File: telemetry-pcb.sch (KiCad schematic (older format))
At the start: 44 parts, among them CN1 12V_IN, CN10 THERMO1, CN11 THERMO2, CN12 RS232, CN13 CAN, CN14 CAN, CN15 12V_OUT, CN16 12V_OUT, CN2 12V_OUT, CN3 12V_OUT, CN5 ACC_12V_CAN, CN6 CAN, CN7 CAN, CN8 CAN, CN9 CAN, IC1 MAX31855K, IC2 MAX31855K, IC3 TCAN332DR, IC4 MAX3232CPWR, M1 MountingHole, M2 MountingHole, M3 MountingHole, M4 MountingHole, T1 TEST_12V, T2 TEST_3V3, T3 TEST_CAN, T4 GPIO1, T5 GPIO2, T6 TEST_RS232

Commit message: finished first draft of PCB
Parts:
- CN10: renamed from CN13; footprint (none) -> Conn_Molex_70553-0001:Molex-70553-0001-0-0-MFG
- CN11: renamed from CN14; footprint (none) -> Conn_Molex_70553-0001:Molex-70553-0001-0-0-MFG
- CN13: renamed from CN10; footprint (none) -> Conn_Molex_70553-0002:Molex-70553-0002-0-0-0; symbol Connector_Generic:Conn_01x02 -> Connector_Generic:Conn_01x03
- CN14: renamed from CN11; footprint (none) -> Conn_Molex_70553-0002:Molex-70553-0002-0-0-0; symbol Connector_Generic:Conn_01x02 -> Connector_Generic:Conn_01x03
- CN6, CN7, CN8, CN9: footprint (none) -> Conn_Molex_70553-0001:Molex-70553-0001-0-0-MFG
- renumbered CN5 to CN12, CN12 to CN15, CN15 to CN4, CN16 to CN5
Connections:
- wire segments 261 -> 259
- no-connect marks 16 -> 18
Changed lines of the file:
@@
 	10100 7150 10100 5750
 $Comp
-L Connector:DB9_Male CN12
+L Connector:DB9_Male CN15
 U 1 1 600D7019
 P 10950 5650
-F 0 "CN12" H 11130 5696 50  0000 L CNN
+F 0 "CN15" H 11130 5696 50  0000 L CNN
 F 1 "RS232" H 11130 5605 50  0000 L CNN
 F 2 "Connector_Dsub:DSUB-9_Male_Horizontal_P2.77x2.54mm_EdgePinOffset9.40mm" H 10950 5650 50  0001 C CNN
@@
 	4950 2500 5700 2500
 Wire Wire Line
-	5250 550  5750 550
-Wire Wire Line
-	6500 1600 6500 850
-Wire Wire Line
-	6500 850  6250 850
-Wire Wire Line
-	6500 850  6500 650
-Wire Wire Line
-	6500 650  6250 650
-Connection ~ 6500 850
-Wire Wire Line
 	8050 2750 8050 2050
-Wire Wire Line
-	6650 1450 6650 750
-Wire Wire Line
-	6650 750  6250 750
 Connection ~ 8050 2750
 Wire Wire Line
-	6650 750  6650 550
-Wire Wire Line
 	6650 550  6250 550
-Connection ~ 6650 750
 $Comp
 L Connector_Generic:Conn_01x02 CN3
@@
 F 0 "CN6" V 7314 112 50  0000 R CNN
 F 1 "CAN" V 7223 112 50  0000 R CNN
-F 2 "" H 7350 300 50  0001 C CNN
+F 2 "Conn_Molex_70553-0001:Molex-70553-0001-0-0-MFG" H 7350 300 50  0001 C CNN
 F 3 "~" H 7350 300 50  0001 C CNN
 	1    7350 300
@@
 F 0 "CN7" V 8114 112 50  0000 R CNN
 F 1 "CAN" V 8023 112 50  0000 R CNN
-F 2 "" H 8150 300 50  0001 C CNN
+F 2 "Conn_Molex_70553-0001:Molex-70553-0001-0-0-MFG" H 8150 300 50  0001 C CNN
 F 3 "~" H 8150 300 50  0001 C CNN
 	1    8150 300
@@
 F 0 "CN8" V 8864 112 50  0000 R CNN
 F 1 "CAN" V 8773 112 50  0000 R CNN
-F 2 "" H 8900 300 50  0001 C CNN
+F 2 "Conn_Molex_70553-0001:Molex-70553-0001-0-0-MFG" H 8900 300 50  0001 C CNN
 F 3 "~" H 8900 300 50  0001 C CNN
 	1    8900 300
@@
 F 0 "CN9" V 9614 112 50  0000 R CNN
 F 1 "CAN" V 9523 112 50  0000 R CNN
-F 2 "" H 9650 300 50  0001 C CNN
+F 2 "Conn_Molex_70553-0001:Molex-70553-0001-0-0-MFG" H 9650 300 50  0001 C CNN
 F 3 "~" H 9650 300 50  0001 C CNN
 	1    9650 300
@@
 Wire Wire Line
 	1300 500  1300 700
-Wire Wire Line
-	2150 500  2150 1200
-Wire Wire Line
-	3000 500  3000 1200
-Connection ~ 2150 1200
-Wire Wire Line
-	2250 1350 2250 500
 Connection ~ 1600 1350
 Wire Wire Line
 	1600 1350 1600 1500
-Wire Wire Line
-	3100 1350 3100 500
-Connection ~ 2250 1350
 $Comp
 L Connector:Conn_01x02_Female T3
@@
 	4950 1900 4950 2050
 $Comp
-L Connector_Generic:Conn_02x05_Counter_Clockwise CN5
+L Connector_Generic:Conn_02x05_Counter_Clockwise CN12
 U 1 1 601BCF89
 P 5950 750
-F 0 "CN5" H 6000 1167 50  0000 C CNN
+F 0 "CN12" H 6000 1167 50  0000 C CNN
 F 1 "ACC_12V_CAN" H 6000 1076 50  0000 C CNN
 F 2 "Connector_Molex:Molex_Mega-Fit_76825-0010_2x05_P5.70mm_Horizontal" H 5950 750 50  0001 C CNN
@@
 	1    0    0    -1
 $EndComp
-Wire Wire Line
-	5250 650  5750 650
-Wire Wire Line
-	5250 750  5750 750
-Wire Wire Line
-	5500 850  5750 850
-Wire Wire Line
-	5500 950  5750 950
-Connection ~ 5500 950
-Wire Wire Line
-	5500 950  5500 850
-$Comp
-L Connector_Generic:Conn_01x02 CN13
+$Comp
+L Connector_Generic:Conn_01x02 CN10
 U 1 1 6024B164
 P 10350 300
-F 0 "CN13" V 10314 112 50  0000 R CNN
+F 0 "CN10" V 10314 112 50  0000 R CNN
 F 1 "CAN" V 10223 112 50  0000 R CNN
-F 2 "" H 10350 300 50  0001 C CNN
+F 2 "Conn_Molex_70553-0001:Molex-70553-0001-0-0-MFG" H 10350 300 50  0001 C CNN
 F 3 "~" H 10350 300 50  0001 C CNN
 	1    10350 300
@@
 $EndComp
 $Comp
-L Connector_Generic:Conn_01x02 CN14
+L Connector_Generic:Conn_01x02 CN11
 U 1 1 6024BB8E
 P 11000 300
-F 0 "CN14" V 10964 112 50  0000 R CNN
+F 0 "CN11" V 10964 112 50  0000 R CNN
 F 1 "CAN" V 10873 112 50  0000 R CNN
-F 2 "" H 11000 300 50  0001 C CNN
+F 2 "Conn_Molex_70553-0001:Molex-70553-0001-0-0-MFG" H 11000 300 50  0001 C CNN
 F 3 "~" H 11000 300 50  0001 C CNN
 	1    11000 300
@@
 $EndComp
 $Comp
-L Connector_Generic:Conn_01x02 CN15
+L Connector_Generic:Conn_01x02 CN4
 U 1 1 6035BAD8
 P 3800 300
-F 0 "CN15" V 3764 112 50  0000 R CNN
+F 0 "CN4" V 3764 112 50  0000 R CNN
 F 1 "12V_OUT" V 3673 112 50  0000 R CNN
 F 2 "Connector_Molex:Molex_Mega-Fit_76825-0002_2x01_P5.70mm_Horizontal" H 3800 300 50  0001 C CNN
@@
 	0    -1   -1   0
 $EndComp
-Wire Wire Line
-	3000 1200 3800 1200
-Wire Wire Line
-	3800 1200 3800 500
-Connection ~ 3000 1200
-Wire Wire Line
-	3100 1350 3900 1350
-Connection ~ 3100 1350
 NoConn ~ 10650 5250
 NoConn ~ 10650 5350
@@
 Connection ~ 4950 2500
 Wire Wire Line
-	3900 500  3900 1350
-Wire Wire Line
-	5500 950  5500 1350
-Wire Wire Line
-	6250 1350 5500 1350
-Wire Wire Line
-	6250 950  6250 1350
-Wire Wire Line
-	3800 1200 4600 1200
-Connection ~ 3800 1200
-Wire Wire Line
 	3000 5500 3000 6200
 Wire Wire Line
@@
 Wire Wire Line
 	3050 6000 2500 6000
-Wire Wire Line
-	2500 6000 2500 5800
 Connection ~ 3050 6000
 $Comp
@@
 Wire Wire Line
 	3050 4900 2500 4900
-Wire Wire Line
-	2500 4900 2500 4700
 Connection ~ 3050 4900
 Wire Wire Line
@@
 	8050 1450 7450 1450
 $Comp
-L Connector_Generic:Conn_01x02 CN16
+L Connector_Generic:Conn_01x02 CN5
 U 1 1 603106BF
 P 4600 300
-F 0 "CN16" V 4564 112 50  0000 R CNN
+F 0 "CN5" V 4564 112 50  0000 R CNN
 F 1 "12V_OUT" V 4473 112 50  0000 R CNN
 F 2 "Connector_Molex:Molex_Mega-Fit_76825-0002_2x01_P5.70mm_Horizontal" H 4600 300 50  0001 C CNN
@@
 	0    -1   -1   0
 $EndComp
-Wire Wire Line
-	4600 500  4600 1200
-Wire Wire Line
-	3900 1350 4700 1350
-Connection ~ 3900 1350
-Wire Wire Line
-	4700 500  4700 1350
-Wire Wire Line
-	4600 1200 5250 1200
-Wire Wire Line
-	5250 1200 5250 750
-Connection ~ 4600 1200
-Connection ~ 5250 650
-Wire Wire Line
-	5250 650  5250 550
-Connection ~ 5250 750
-Wire Wire Line
-	5250 750  5250 650
-Wire Wire Line
-	4700 1350 5500 1350
-Connection ~ 4700 1350
-Connection ~ 5500 1350
 Wire Wire Line
 	1400 500  1400 600
@@
 $EndComp
 $Comp
-L Connector_Generic:Conn_01x02 CN10
+L Connector_Generic:Conn_01x03 CN14
+U 1 1 601BC25C
+P 2300 5800
+F 0 "CN14" V 2264 5612 50  0000 R CNN
+F 1 "THERMO2" V 2173 5612 50  0000 R CNN
+F 2 "Conn_Molex_70553-0002:Molex-70553-0002-0-0-0" H 2300 5800 50  0001 C CNN
+F 3 "~" H 2300 5800 50  0001 C CNN
+	1    2300 5800
+	-1   0    0    1
+$EndComp
+Connection ~ 1400 700
+Wire Wire Line
+	1400 1000 1400 1200
+Wire Wire Line
+	1200 1350 1200 500
+Wire Wire Line
+	1200 1350 1100 1350
+Connection ~ 1200 1350
+Wire Wire Line
+	1100 500  1100 600
+Wire Wire Line
+	750  1350 1100 1350
+Connection ~ 1100 1350
+Wire Wire Line
+	750  1250 750  1200
+Wire Wire Line
+	750  1200 1400 1200
+Connection ~ 1400 1200
+Connection ~ 1400 600
+Wire Wire Line
+	1400 600  1400 700
+Connection ~ 1100 600
+Wire Wire Line
+	1100 600  1100 1350
+Wire Wire Line
+	1400 1200 1850 1200
+Wire Wire Line
+	1850 1100 1850 1200
+Connection ~ 1850 1200
+Wire Wire Line
+	2500 4800 2500 4900
+Wire Wire Line
+	2500 5900 2500 6000
+NoConn ~ 2500 4700
+NoConn ~ 2500 5800
+$Comp
+L Connector_Generic:Conn_01x03 CN13
 U 1 1 60178289
 P 2300 4700
-F 0 "CN10" V 2264 4512 50  0000 R CNN
+F 0 "CN13" V 2264 4512 50  0000 R CNN
 F 1 "THERMO1" V 2173 4512 50  0000 R CNN
-F 2 "" H 2300 4700 50  0001 C CNN
+F 2 "Conn_Molex_70553-0002:Molex-70553-0002-0-0-0" H 2300 4700 50  0001 C CNN
 F 3 "~" H 2300 4700 50  0001 C CNN
 	1    2300 4700
 	-1   0    0    1
 $EndComp
-$Comp
-L Connector_Generic:Conn_01x02 CN11
-U 1 1 601BC25C
-P 2300 5800
-F 0 "CN11" V 2264 5612 50  0000 R CNN
-F 1 "THERMO2" V 2173 5612 50  0000 R CNN
-F 2 "" H 2300 5800 50  0001 C CNN
-F 3 "~" H 2300 5800 50  0001 C CNN
-	1    2300 5800
-	-1   0    0    1
-$EndComp
-Connection ~ 1400 700
-Wire Wire Line
-	1400 1000 1400 1200
-Wire Wire Line
-	1200 1350 1200 500
-Wire Wire Line
-	1200 1350 1100 1350
-Connection ~ 1200 1350
-Wire Wire Line
-	1100 500  1100 600
-Wire Wire Line
-	1600 1350 2250 1350
-Wire Wire Line
-	750  1350 1100 1350
-Connection ~ 1100 1350
-Wire Wire Line
-	750  1250 750  1200
-Wire Wire Line
-	750  1200 1400 1200
-Connection ~ 1400 1200
-Wire Wire Line
-	2250 1350 3100 1350
-Connection ~ 1400 600
-Wire Wire Line
-	1400 600  1400 700
-Wire Wire Line
-	2150 1200 3000 1200
-Connection ~ 1100 600
-Wire Wire Line
-	1100 600  1100 1350
-Wire Wire Line
-	1400 1200 1850 1200
-Wire Wire Line
-	1850 1100 1850 1200
-Connection ~ 1850 1200
-Wire Wire Line
-	1850 1200 2150 1200
+Wire Wire Line
+	6650 550  6650 1450
+Wire Wire Line
+	6500 1600 6500 650
+Wire Wire Line
+	6500 650  6250 650
+Wire Wire Line
+	6500 1600 5650 1600
+Wire Wire Line
+	5650 1600 5650 850
+Wire Wire Line
+	5650 850  5750 850
+Connection ~ 6500 1600
+Wire Wire Line
+	6650 1450 5750 1450
+Wire Wire Line
+	5750 1450 5750 950
+Connection ~ 6650 1450
+Wire Wire Line
+	1600 1350 2150 1350
+Wire Wire Line
+	1850 1200 2250 1200
+Wire Wire Line
+	2150 500  2150 1350
+Connection ~ 2150 1350
+Wire Wire Line
+	2150 1350 3000 1350
+Wire Wire Line
+	2250 500  2250 1200
+Connection ~ 2250 1200
+Wire Wire Line
+	2250 1200 3100 1200
+Wire Wire Line
+	3000 500  3000 1350
+Connection ~ 3000 1350
+Wire Wire Line
+	3000 1350 3800 1350
+Wire Wire Line
+	3100 500  3100 1200
+Connection ~ 3100 1200
+Wire Wire Line
+	3100 1200 3900 1200
+Wire Wire Line
+	3800 500  3800 1350
+Connection ~ 3800 1350
+Wire Wire Line
+	3800 1350 4600 1350
+Wire Wire Line
+	3900 500  3900 1200
+Connection ~ 3900 1200
+Wire Wire Line
+	3900 1200 4700 1200
+Wire Wire Line
+	4600 500  4600 1350
+Connection ~ 4600 1350
+Wire Wire Line
+	4700 500  4700 1200
+Connection ~ 4700 1200
+Wire Wire Line
+	4600 1350 5550 1350
+Wire Wire Line
+	4700 1200 6250 1200
+Wire Wire Line
+	6250 1200 6250 950
+Wire Wire Line
+	6250 850  6250 750
+Wire Wire Line
+	6250 850  6250 950
+Connection ~ 6250 850
+Connection ~ 6250 950
+Wire Wire Line
+	5550 1350 5550 750
+Wire Wire Line
+	5550 750  5750 750
+Wire Wire Line
+	5550 750  5550 650
+Wire Wire Line
+	5550 550  5750 550
+Connection ~ 5550 750
+Wire Wire Line
+	5750 650  5550 650
+Connection ~ 5550 650
+Wire Wire Line
+	5550 650  5550 550
 $EndSCHEMATC

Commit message: cleaned up repo
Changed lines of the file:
@@
 L power:PWR_FLAG #FLG0101
 U 1 1 6065A11D
-P 1400 600
-F 0 "#FLG0101" H 1400 675 50  0001 C CNN
-F 1 "PWR_FLAG" V 1400 727 50  0000 L CNN
-F 2 "" H 1400 600 50  0001 C CNN
-F 3 "~" H 1400 600 50  0001 C CNN
-	1    1400 600
-	0    1    1    0
+P 1700 1200
+F 0 "#FLG0101" H 1700 1275 50  0001 C CNN
+F 1 "PWR_FLAG" V 1700 1327 50  0000 L CNN
+F 2 "" H 1700 1200 50  0001 C CNN
+F 3 "~" H 1700 1200 50  0001 C CNN
+	1    1700 1200
+	1    0    0    -1
 $EndComp
 $Comp
@@
 	0    -1   -1   0
 $EndComp
-Wire Wire Line
-	1400 500  1400 600
 $Comp
 L Mechanical:MountingHole M2
@@
 	1    0    0    -1
 $EndComp
-Wire Wire Line
-	400  2600 400  3900
 $Comp
 L Mechanical:MountingHole M1
@@
 	750  1200 1400 1200
 Connection ~ 1400 1200
-Connection ~ 1400 600
-Wire Wire Line
-	1400 600  1400 700
 Connection ~ 1100 600
 Wire Wire Line
 	1100 600  1100 1350
 Wire Wire Line
-	1400 1200 1850 1200
+	1400 1200 1700 1200
 Wire Wire Line
 	1850 1100 1850 1200
@@
 Wire Wire Line
 	5550 650  5550 550
+Connection ~ 1700 1200
+Wire Wire Line
+	1700 1200 1850 1200
+Wire Wire Line
+	1400 500  1400 700
+Wire Wire Line
+	400  2600 400  3900
 $EndSCHEMATC

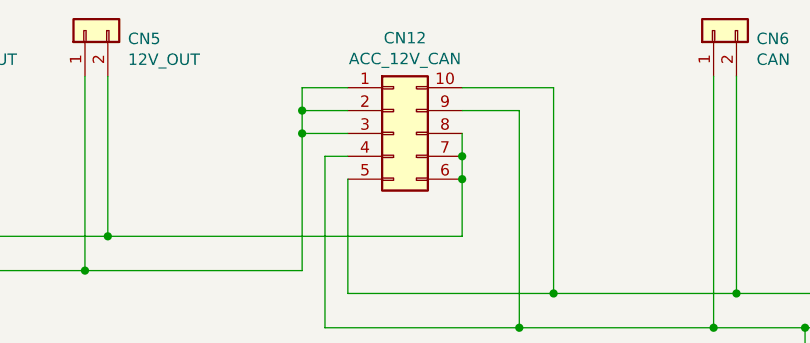
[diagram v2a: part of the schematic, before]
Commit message: added references to silkscreen and fixed Molex SL footprint soldermask
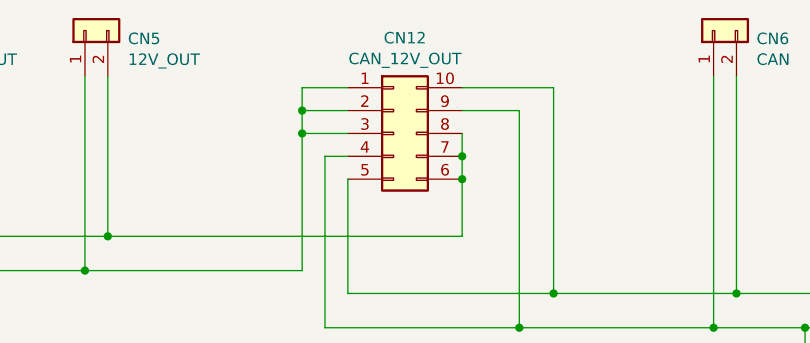
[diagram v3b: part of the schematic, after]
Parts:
- CN12: value ACC_12V_CAN -> CAN_12V_OUT
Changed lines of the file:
@@
 Text Label 5750 6250 0    50   ~ 0
 VIN
-$Comp
-L Connector:Conn_01x18_Female T4
-U 1 1 601E1414
-P 6100 7050
-F 0 "T4" H 6128 7026 50  0000 L CNN
-F 1 "GPIO1" H 6128 6935 50  0000 L CNN
-F 2 "Connector_PinHeader_2.54mm:PinHeader_1x18_P2.54mm_Vertical" H 6100 7050 50  0001 C CNN
-F 3 "~" H 6100 7050 50  0001 C CNN
-	1    6100 7050
-	1    0    0    -1
-$EndComp
 Wire Wire Line
 	5900 6250 5750 6250
@@
 Wire Wire Line
 	5900 7950 5750 7950
-$Comp
-L Connector:Conn_01x18_Female T5
-U 1 1 60259DFD
-P 6900 7050
-F 0 "T5" H 6928 7026 50  0000 L CNN
-F 1 "GPIO2" H 6928 6935 50  0000 L CNN
-F 2 "Connector_PinHeader_2.54mm:PinHeader_1x18_P2.54mm_Vertical" H 6900 7050 50  0001 C CNN
-F 3 "~" H 6900 7050 50  0001 C CNN
-	1    6900 7050
-	1    0    0    -1
-$EndComp
 Wire Wire Line
 	6700 6250 6550 6250
@@
 Wire Wire Line
 	2750 5500 3000 5500
-$Comp
-L telemetry-pcb-eagle-import:ELECTRON_WITH_HEADERS H2,H3
-U 1 1 4D826FCC
-P 6400 4200
-F 0 "H2,H3" H 6400 4050 50  0000 C CNN
-F 1 "ELECTRON" H 6400 4350 50  0000 C CNN
-F 2 "Libraries:electron" H 6400 4200 50  0001 C CNN
-F 3 "" H 6400 4200 50  0001 C CNN
-	1    6400 4200
-	1    0    0    -1
-$EndComp
 Wire Wire Line
 	4300 5800 5400 5800
@@
 P 5950 750
 F 0 "CN12" H 6000 1167 50  0000 C CNN
-F 1 "ACC_12V_CAN" H 6000 1076 50  0000 C CNN
+F 1 "CAN_12V_OUT" H 6000 1076 50  0000 C CNN
 F 2 "Connector_Molex:Molex_Mega-Fit_76825-0010_2x05_P5.70mm_Horizontal" H 5950 750 50  0001 C CNN
 F 3 "~" H 5950 750 50  0001 C CNN
@@
 Wire Wire Line
 	400  2600 400  3900
+$Comp
+L telemetry-pcb-eagle-import:ELECTRON_WITH_HEADERS H2,H3
+U 1 1 4D826FCC
+P 6400 4200
+F 0 "H2,H3" H 6400 4050 50  0000 C CNN
+F 1 "ELECTRON" H 6400 4350 50  0000 C CNN
+F 2 "Libraries:electron" H 6400 4200 50  0001 C CNN
+F 3 "" H 6400 4200 50  0001 C CNN
+	1    6400 4200
+	1    0    0    -1
+$EndComp
+$Comp
+L Connector:Conn_01x18_Female T5
+U 1 1 60259DFD
+P 6900 7050
+F 0 "T5" H 6928 7026 50  0000 L CNN
+F 1 "GPIO2" H 6928 6935 50  0000 L CNN
+F 2 "Connector_PinHeader_2.54mm:PinHeader_1x18_P2.54mm_Vertical" H 6900 7050 50  0001 C CNN
+F 3 "~" H 6900 7050 50  0001 C CNN
+	1    6900 7050
+	1    0    0    -1
+$EndComp
+$Comp
+L Connector:Conn_01x18_Female T4
+U 1 1 601E1414
+P 6100 7050
+F 0 "T4" H 6128 7026 50  0000 L CNN
+F 1 "GPIO1" H 6128 6935 50  0000 L CNN
+F 2 "Connector_PinHeader_2.54mm:PinHeader_1x18_P2.54mm_Vertical" H 6100 7050 50  0001 C CNN
+F 3 "~" H 6100 7050 50  0001 C CNN
+	1    6100 7050
+	1    0    0    -1
+$EndComp
 $EndSCHEMATC
